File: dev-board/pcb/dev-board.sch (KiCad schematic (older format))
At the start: 50 parts, among them J1 Raspberry_Pi_2_3, J2 USB_B_Micro, Q1 BSS84, Q2 BSS84, U1 MCP2210-I-SS, U2 TPS2115APW, U3 MIC5504-3.3YM5, U4 CD74HC154, Y1 12MHz

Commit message: Use "10k" resistor value consistently
Otherwise the BOM creates an extra group that isn't needed.
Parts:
- R1: value 10K -> 10k
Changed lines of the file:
@@
 P 9000 2500
 F 0 "R1" H 9070 2546 50  0000 L CNN
-F 1 "10K" H 9070 2455 50  0000 L CNN
+F 1 "10k" H 9070 2455 50  0000 L CNN
 F 2 "Capacitor_SMD:C_0805_2012Metric_Pad1.15x1.40mm_HandSolder" V 8930 2500 50  0001 C CNN
 F 3 "~" H 9000 2500 50  0001 C CNN

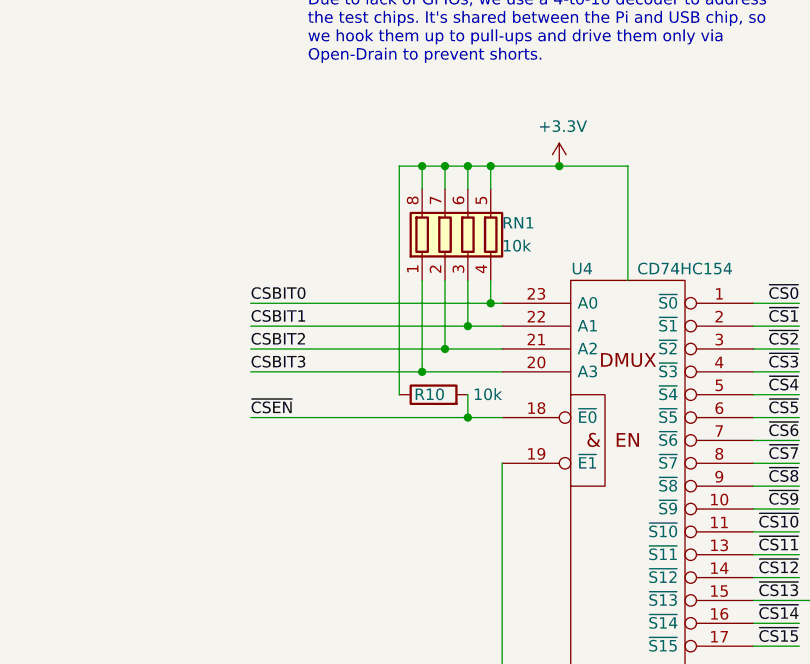
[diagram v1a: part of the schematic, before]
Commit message: Replace RN1 with 4 0804 resistors
Closes #9
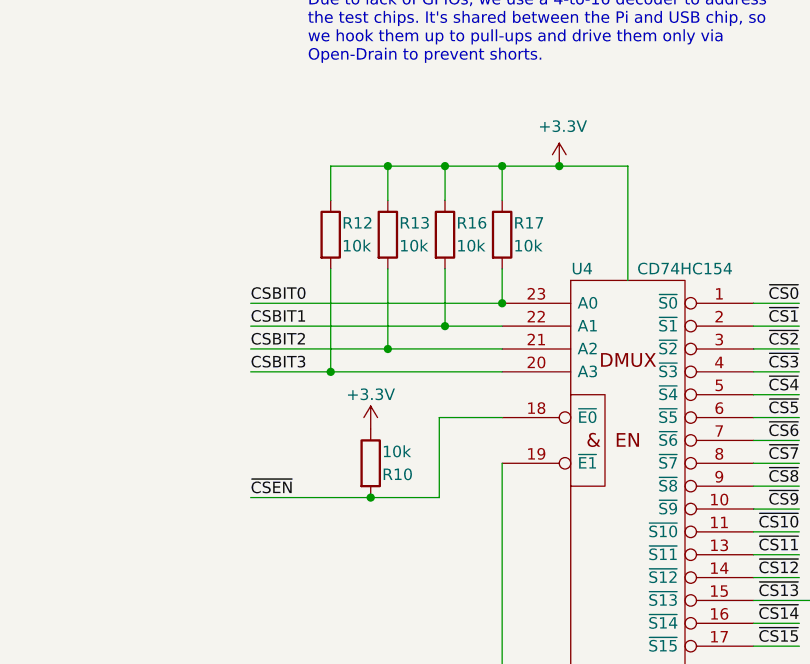
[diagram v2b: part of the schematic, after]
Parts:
- removed RN1: 10k, Resistor_SMD:R_Array_Convex_4x0603, symbol Device:R_Pack04
- added R12, R13, R16, R17: 10k, Capacitor_SMD:C_0805_2012Metric_Pad1.15x1.40mm_HandSolder, symbol Device:R
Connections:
- net +3V3: now also R12.1, R13.1, R16.1, R17.1
- net CSBIT0: now also R17.2
- net CSBIT1: now also R16.2
- net CSBIT2: now also R13.2
- net CSBIT3: now also R12.2
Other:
- moved on the sheet: R10
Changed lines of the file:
@@
 Text Label 4350 6900 0    50   ~ 0
 CSBIT3
-Text Label 4350 7100 0    50   ~ 0
-~CSEN
 $Comp
 L power:+3.3V #PWR021
@@
 Wire Wire Line
 	6000 6000 5700 6000
-Wire Wire Line
-	5700 6000 5400 6000
-Wire Wire Line
-	5400 6000 5400 6100
 Connection ~ 5700 6000
-Wire Wire Line
-	5400 6000 5300 6000
-Wire Wire Line
-	5300 6000 5300 6100
-Connection ~ 5400 6000
-Wire Wire Line
-	5300 6000 5200 6000
-Wire Wire Line
-	5200 6000 5200 6100
-Connection ~ 5300 6000
-Wire Wire Line
-	5200 6000 5100 6000
-Wire Wire Line
-	5100 6000 5100 6100
-Connection ~ 5200 6000
-Wire Wire Line
-	4350 7100 5300 7100
-Wire Wire Line
-	5450 6900 5100 6900
-Wire Wire Line
-	4350 6800 5200 6800
-Wire Wire Line
-	5450 6700 5300 6700
-Wire Wire Line
-	4350 6600 5400 6600
-Wire Wire Line
-	5400 6500 5400 6600
-Connection ~ 5400 6600
-Wire Wire Line
-	5400 6600 5450 6600
-Wire Wire Line
-	5300 6500 5300 6700
-Connection ~ 5300 6700
-Wire Wire Line
-	5300 6700 4350 6700
-Wire Wire Line
-	5200 6500 5200 6800
-Connection ~ 5200 6800
-Wire Wire Line
-	5200 6800 5450 6800
-Wire Wire Line
-	5100 6500 5100 6900
-Connection ~ 5100 6900
-Wire Wire Line
-	5100 6900 4350 6900
 Wire Wire Line
 	5450 7300 5450 8300
@@
 L Device:R R10
 U 1 1 5DC83C87
-P 5150 7000
-F 0 "R10" V 5150 6950 50  0000 L CNN
-F 1 "10k" V 5150 6700 50  0000 L CNN
-F 2 "Capacitor_SMD:C_0805_2012Metric_Pad1.15x1.40mm_HandSolder" V 5080 7000 50  0001 C CNN
-F 3 "~" H 5150 7000 50  0001 C CNN
-	1    5150 7000
-	0    -1   -1   0
-$EndComp
-Wire Wire Line
-	5300 7000 5300 7100
-Connection ~ 5300 7100
-Wire Wire Line
-	5300 7100 5450 7100
-Wire Wire Line
-	5000 7000 5000 6000
-Wire Wire Line
-	5000 6000 5100 6000
-Connection ~ 5100 6000
+P 4875 7300
+F 0 "R10" H 4925 7250 50  0000 L CNN
+F 1 "10k" H 4925 7350 50  0000 L CNN
+F 2 "Capacitor_SMD:C_0805_2012Metric_Pad1.15x1.40mm_HandSolder" V 4805 7300 50  0001 C CNN
+F 3 "~" H 4875 7300 50  0001 C CNN
+	1    4875 7300
+	1    0    0    -1
+$EndComp
 Text Label 10500 3950 2    50   ~ 0
 CSBIT0
@@
 Wire Wire Line
 	13250 2150 13550 2150
-$Comp
-L Device:R_Pack04 RN1
-U 1 1 5DBC682D
-P 5300 6300
-F 0 "RN1" H 5450 6350 50  0000 L CNN
-F 1 "10k" H 5450 6250 50  0000 L CNN
-F 2 "Resistor_SMD:R_Array_Convex_4x0603" V 5575 6300 50  0001 C CNN
-F 3 "~" H 5300 6300 50  0001 C CNN
-	1    5300 6300
-	1    0    0    -1
-$EndComp
 $Sheet
 S 8650 6500 700  400
@@
 Text Notes 7150 7900 0    25   ~ 0
 FIXME: CS13 is wrongly marked as\nan input to the decoder, so I placed\na power flag to keep DRC quiet.
+Wire Wire Line
+	4350 6600 5450 6600
+$Comp
+L Device:R R17
+U 1 1 5DA89E23
+P 5450 6300
+F 0 "R17" H 5500 6350 50  0000 L CNN
+F 1 "10k" H 5500 6250 50  0000 L CNN
+F 2 "Capacitor_SMD:C_0805_2012Metric_Pad1.15x1.40mm_HandSolder" V 5380 6300 50  0001 C CNN
+F 3 "~" H 5450 6300 50  0001 C CNN
+	1    5450 6300
+	1    0    0    -1
+$EndComp
+Wire Wire Line
+	5450 6450 5450 6600
+Connection ~ 5450 6600
+Wire Wire Line
+	5450 6150 5450 6000
+Connection ~ 5450 6000
+Wire Wire Line
+	5450 6000 5700 6000
+Wire Wire Line
+	4350 6800 4950 6800
+Wire Wire Line
+	4350 6900 4700 6900
+$Comp
+L Device:R R16
+U 1 1 5DADFCBE
+P 5200 6300
+F 0 "R16" H 5250 6350 50  0000 L CNN
+F 1 "10k" H 5250 6250 50  0000 L CNN
+F 2 "Capacitor_SMD:C_0805_2012Metric_Pad1.15x1.40mm_HandSolder" V 5130 6300 50  0001 C CNN
+F 3 "~" H 5200 6300 50  0001 C CNN
+	1    5200 6300
+	1    0    0    -1
+$EndComp
+Wire Wire Line
+	4350 6700 5200 6700
+Wire Wire Line
+	5200 6450 5200 6700
+Connection ~ 5200 6700
+Wire Wire Line
+	5200 6700 5450 6700
+Wire Wire Line
+	5200 6150 5200 6000
+Connection ~ 5200 6000
+Wire Wire Line
+	5200 6000 5450 6000
+Text Label 4350 7450 0    50   ~ 0
+~CSEN
+Wire Wire Line
+	5175 7100 5450 7100
+$Comp
+L power:+3.3V #PWR025
+U 1 1 5DBC7191
+P 4875 7150
+F 0 "#PWR025" H 4875 7000 50  0001 C CNN
+F 1 "+3.3V" H 4875 7300 50  0000 C CNN
+F 2 "" H 4875 7150 50  0001 C CNN
+F 3 "" H 4875 7150 50  0001 C CNN
+	1    4875 7150
+	1    0    0    -1
+$EndComp
+$Comp
+L Device:R R13
+U 1 1 5DC03440
+P 4950 6300
+F 0 "R13" H 5000 6350 50  0000 L CNN
+F 1 "10k" H 5000 6250 50  0000 L CNN
+F 2 "Capacitor_SMD:C_0805_2012Metric_Pad1.15x1.40mm_HandSolder" V 4880 6300 50  0001 C CNN
+F 3 "~" H 4950 6300 50  0001 C CNN
+	1    4950 6300
+	1    0    0    -1
+$EndComp
+$Comp
+L Device:R R12
+U 1 1 5DC204B4
+P 4700 6300
+F 0 "R12" H 4750 6350 50  0000 L CNN
+F 1 "10k" H 4750 6250 50  0000 L CNN
+F 2 "Capacitor_SMD:C_0805_2012Metric_Pad1.15x1.40mm_HandSolder" V 4630 6300 50  0001 C CNN
+F 3 "~" H 4700 6300 50  0001 C CNN
+	1    4700 6300
+	1    0    0    -1
+$EndComp
+Wire Wire Line
+	4950 6450 4950 6800
+Connection ~ 4950 6800
+Wire Wire Line
+	4950 6800 5450 6800
+Wire Wire Line
+	4950 6000 4950 6150
+Wire Wire Line
+	4950 6000 5200 6000
+Wire Wire Line
+	4950 6000 4700 6000
+Wire Wire Line
+	4700 6000 4700 6150
+Connection ~ 4950 6000
+Wire Wire Line
+	4700 6450 4700 6900
+Connection ~ 4700 6900
+Wire Wire Line
+	4700 6900 5450 6900
+Wire Wire Line
+	5175 7100 5175 7450
+Wire Wire Line
+	4875 7450 5175 7450
+Wire Wire Line
+	4350 7450 4875 7450
+Connection ~ 4875 7450
 $EndSCHEMATC
